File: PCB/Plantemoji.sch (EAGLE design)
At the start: 34 parts, among them IC3 MEGA8-P, Q1 TIP120, Q2 TIP120

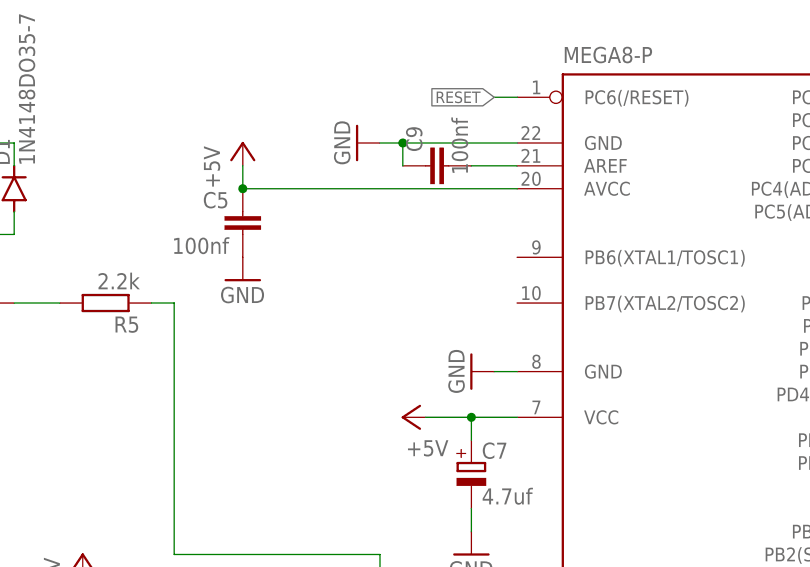
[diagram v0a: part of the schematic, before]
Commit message: PCB is sent to PCBWay! Gerber files were generated using this tutorial (https://www.pcbway.com/helpcenter/technical_support/Generate_Gerber_files_in_Eagle.html)
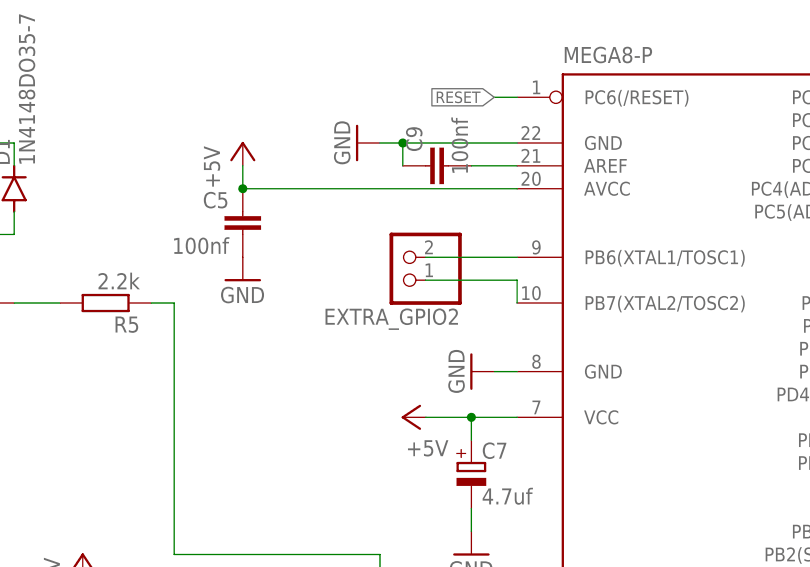
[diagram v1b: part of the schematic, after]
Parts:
- added EXTRA_GPIO2: (no value), pinhead:PINHD-1X2
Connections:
- new net N$33: EXTRA_GPIO2.2, IC3.PB6(XTAL1/TOSC1)
- new net N$34: EXTRA_GPIO2.1, IC3.PB7(XTAL2/TOSC2)
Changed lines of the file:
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@@
 <part name="EXTRA_GPIO" library="pinhead" library_urn="urn:adsk.eagle:library:325" deviceset="PINHD-1X2" device="" package3d_urn="urn:adsk.eagle:package:22435/2"/>
 <part name="P+15" library="supply1" deviceset="+5V" device=""/>
+<part name="EXTRA_GPIO2" library="pinhead" library_urn="urn:adsk.eagle:library:325" deviceset="PINHD-1X2" device="" package3d_urn="urn:adsk.eagle:package:22435/2"/>
 </parts>
 <sheets>
@@
 <instance part="P+15" gate="1" x="139.7" y="162.56" smashed="yes">
 <attribute name="VALUE" x="137.16" y="157.48" size="1.778" layer="96" rot="R90"/>
+</instance>
+<instance part="EXTRA_GPIO2" gate="G$1" x="30.48" y="99.06" smashed="yes" rot="R180">
+<attribute name="NAME" x="36.83" y="93.345" size="1.778" layer="95" rot="R180"/>
+<attribute name="VALUE" x="36.83" y="104.14" size="1.778" layer="96" rot="R180"/>
 </instance>
 </instances>
@@
 </segment>
 </net>
+<net name="N$33" class="0">
+<segment>
+<pinref part="IC3" gate="G$1" pin="PB6(XTAL1/TOSC1)"/>
+<pinref part="EXTRA_GPIO2" gate="G$1" pin="2"/>
+<wire x1="43.18" y1="99.06" x2="33.02" y2="99.06" width="0.1524" layer="91"/>
+</segment>
+</net>
+<net name="N$34" class="0">
+<segment>
+<pinref part="IC3" gate="G$1" pin="PB7(XTAL2/TOSC2)"/>
+<pinref part="EXTRA_GPIO2" gate="G$1" pin="1"/>
+<wire x1="43.18" y1="93.98" x2="43.18" y2="96.52" width="0.1524" layer="91"/>
+<wire x1="43.18" y1="96.52" x2="33.02" y2="96.52" width="0.1524" layer="91"/>
+</segment>
+</net>

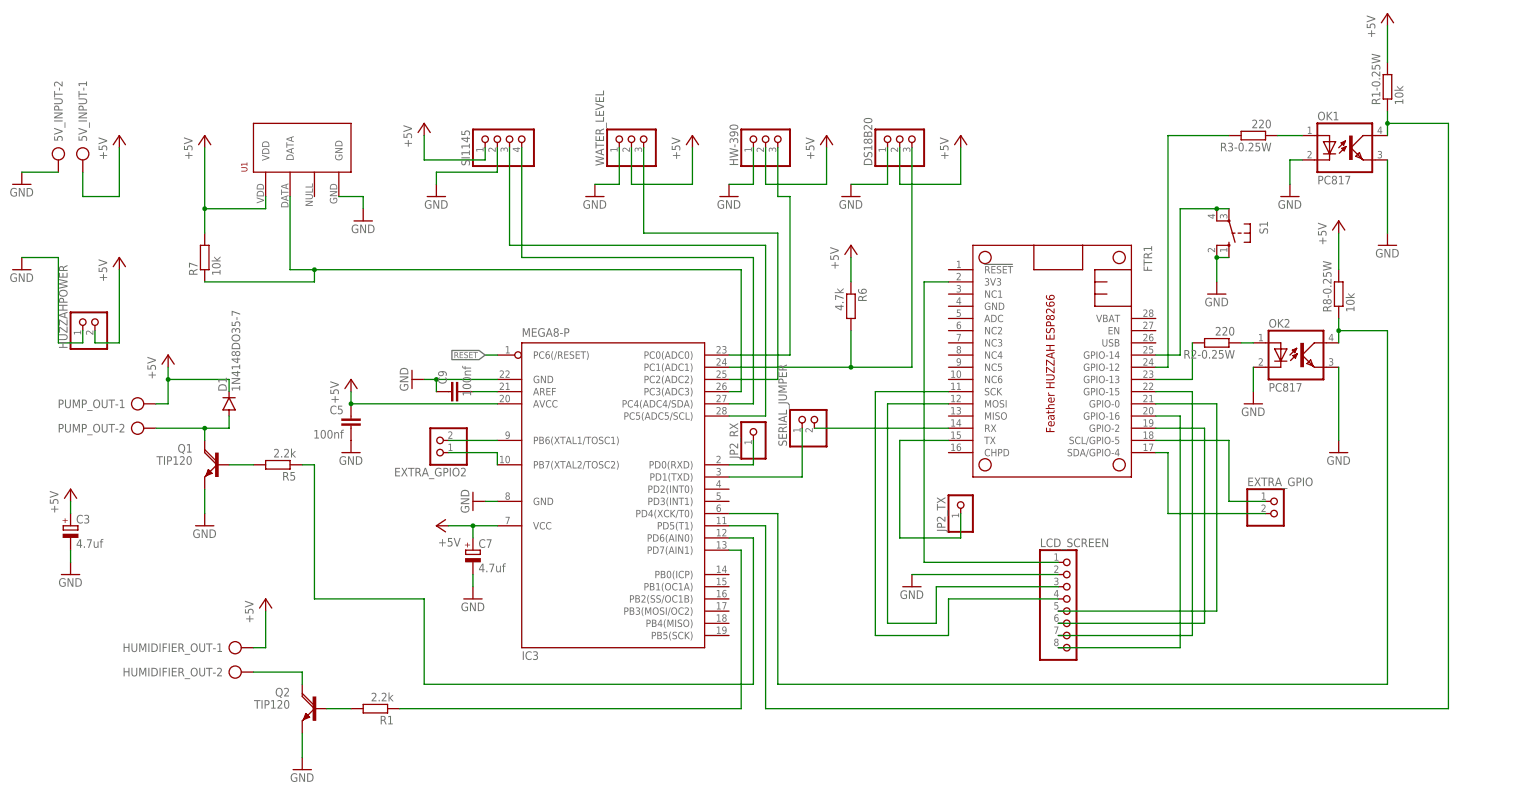
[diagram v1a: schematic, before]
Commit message: Major update to the PCB: now it's based on ESP32 (FireBeetle) instead of the old ESP8266 (Feather Huzzah)
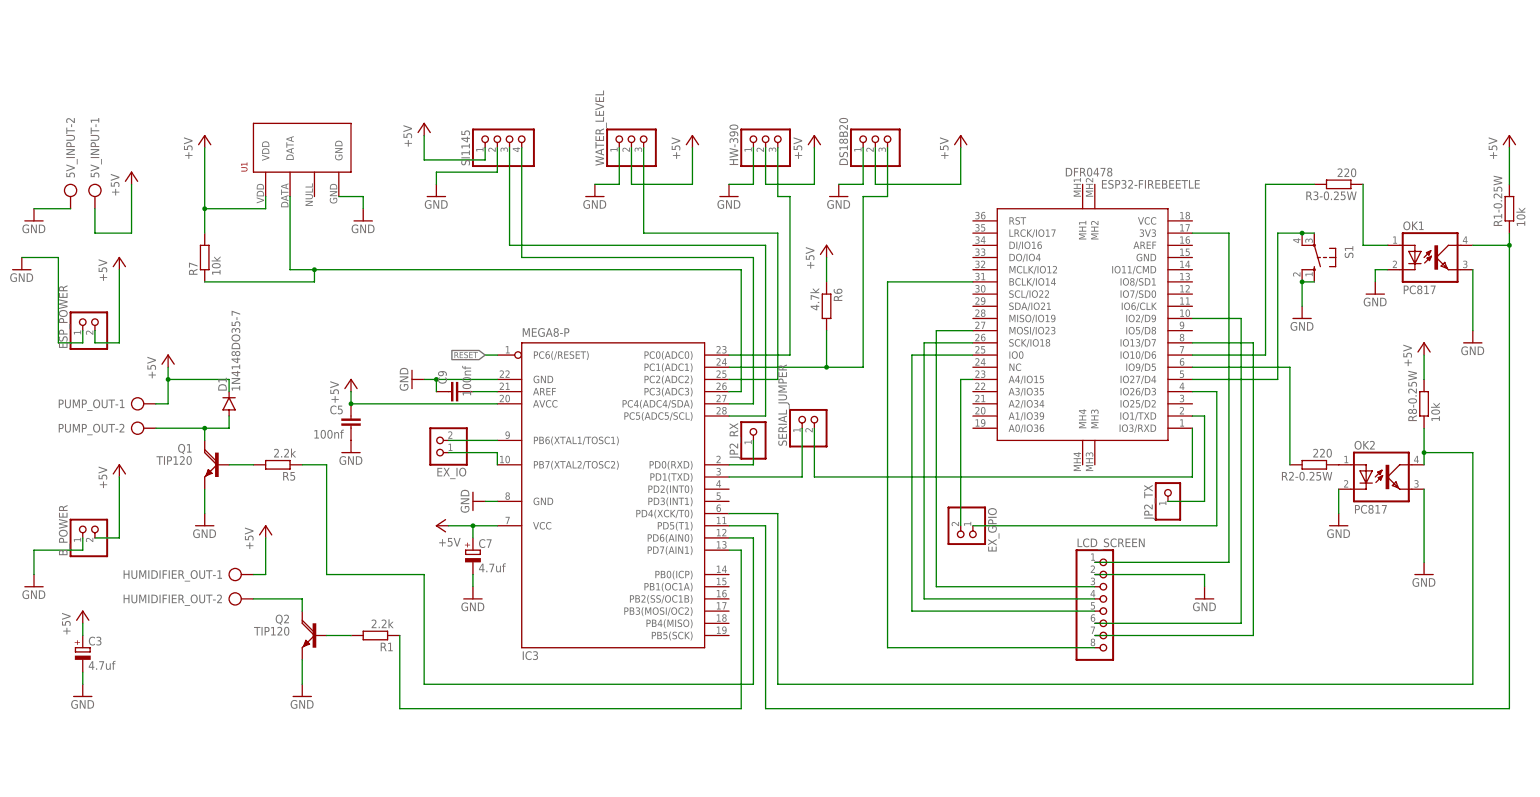
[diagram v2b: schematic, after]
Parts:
- removed EXTRA_GPIO: (no value), pinhead:PINHD-1X2
- removed FTR1: FEATHER_HUZZAH_ESP8266, adafruit-supplemental-arkane:FEATHER_HUZZAH_ESP8266
- added B_POWER, EX_GPIO: (no value), pinhead:PINHD-1X2
- added ESP32-FIREBEETLE: DFR0478, DFR0478:DFR0478
- renumbered EXTRA_GPIO2 to EX_IO, HUZZAHPOWER to ESP_POWER
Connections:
- removed net 3V3: FTR1.3V3, LCD_SCREEN.1
- new net N$35: ESP32-FIREBEETLE.IO26/D3, EX_GPIO.1
- net +5V: now also B_POWER.2
- net GND: now also B_POWER.1
- net N$10: now also ESP32-FIREBEETLE.IO2/D9, LCD_SCREEN.6; no longer FTR1.GPIO-16, LCD_SCREEN.8
- net N$13: now also ESP32-FIREBEETLE.IO9/D5; no longer FTR1.GPIO-13
- net N$16: now also ESP32-FIREBEETLE.IO10/D6; no longer FTR1.GPIO-12
- net N$18: now also ESP32-FIREBEETLE.IO1/TXD; no longer FTR1.TX
- net N$2: now also ESP32-FIREBEETLE.IO27/D4; no longer FTR1.GPIO-14
- net N$31: now also ESP32-FIREBEETLE.BCLK/IO14, LCD_SCREEN.8; no longer EXTRA_GPIO.1, FTR1.SCL/GPIO-5
- net N$32: now also ESP32-FIREBEETLE.A4/IO15, EX_GPIO.2; no longer EXTRA_GPIO.2, FTR1.SDA/GPIO-4
- net N$4: now also ESP32-FIREBEETLE.IO3/RXD; no longer FTR1.RX
- net N$5: now also ESP32-FIREBEETLE.3V3, LCD_SCREEN.1; no longer FTR1.MOSI, LCD_SCREEN.3
- net N$6: now also ESP32-FIREBEETLE.MOSI/IO23, LCD_SCREEN.3; no longer FTR1.SCK, LCD_SCREEN.4
- net N$7: now also ESP32-FIREBEETLE.SCK/IO18, LCD_SCREEN.4; no longer FTR1.GPIO-0, LCD_SCREEN.5
- net N$8: now also ESP32-FIREBEETLE.IO13/D7, LCD_SCREEN.7; no longer FTR1.GPIO-2, LCD_SCREEN.6
- net N$9: now also ESP32-FIREBEETLE.IO0, LCD_SCREEN.5; no longer FTR1.GPIO-15, LCD_SCREEN.7
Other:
- moved on the sheet: 5V_INPUT-1, 5V_INPUT-2, C3, DS18B20, HUMIDIFIER_OUT-1, HUMIDIFIER_OUT-2, JP2_TX, LCD_SCREEN, OK1, OK2, Q2, R1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
